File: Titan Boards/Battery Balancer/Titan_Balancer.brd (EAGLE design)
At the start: 101.6 x 101.6 mm, 86 parts, among them IC1 REG1117, P1 39-30-04?, P2 39-30-10?, P3 39-30-10?, Q1 SPD30P06PTO252, Q12 310mA/60V/1.6Ω, Q2 SPB80P06P, Q3 SPB80P06P, Q4 SPD30P06PTO252, U1 I6A4W020A033V-001-R, U2 I6A4W020A033V-001-R

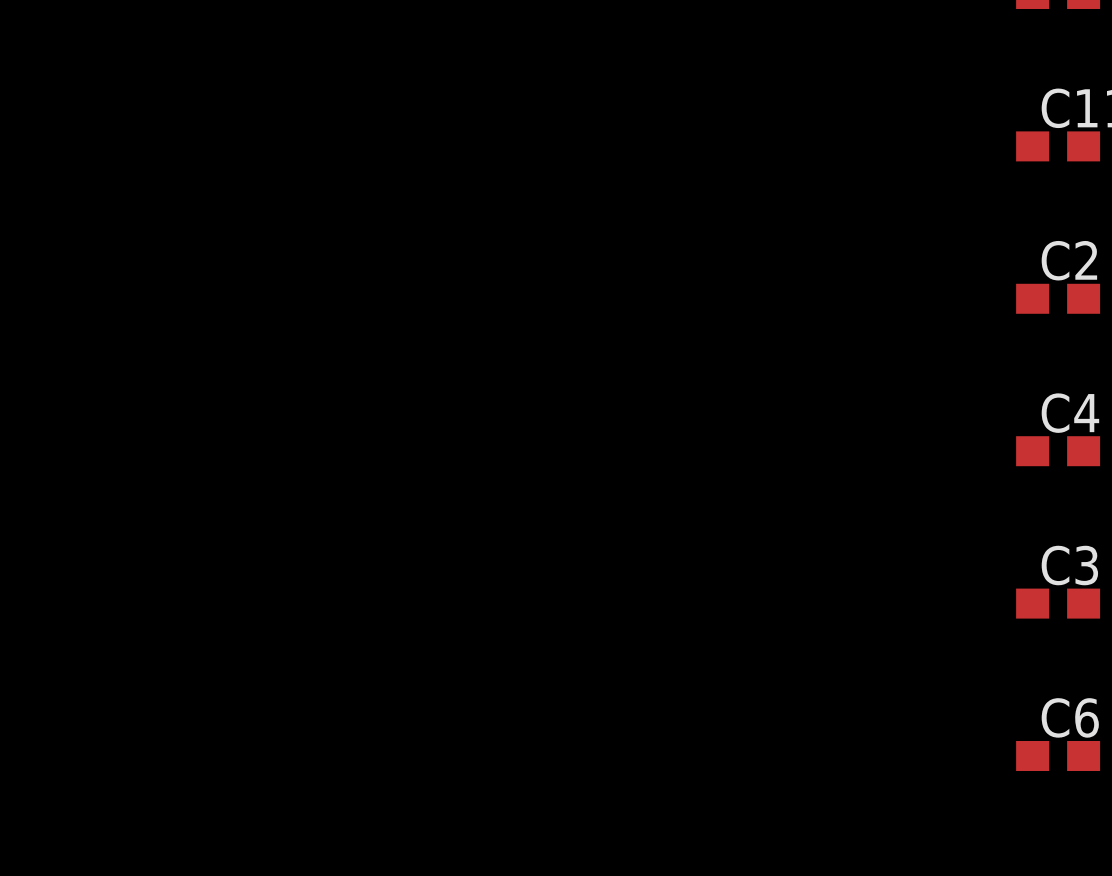
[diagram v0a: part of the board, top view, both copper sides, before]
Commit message: Seperated fan and lighting and added web addresses
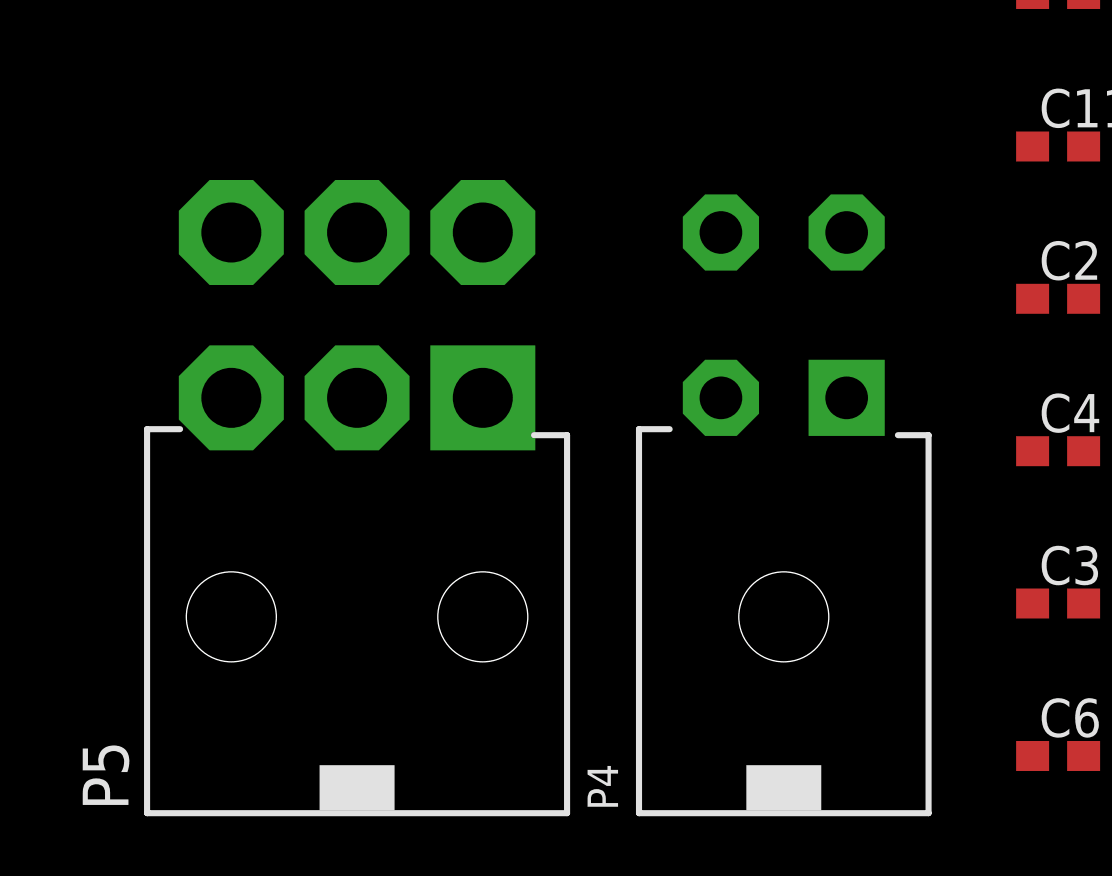
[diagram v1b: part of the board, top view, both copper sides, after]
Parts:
- added P4: 39-30-04?, con-molex-mini-fit:39-30-?04?
- added P5: 39-30-06?, con-molex-mini-fit:39-30-?06?
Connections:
- new net LIGHTING_1.1: P5.1
- new net LIGHTING_2.1: P5.6
- net +12V: now also P5.2, P5.3, P5.4, P5.5
- net GND: now also P4.1, P4.2, P4.3, P4.4
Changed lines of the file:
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@@
 <attribute name="VALUE" x="0.889" y="-187.833" size="1.27" layer="27"/>
+</element>
+<element name="P4" library="con-molex-mini-fit" package="39-30-?04?" value="39-30-04?" x="-7.62" y="-173.99" smashed="yes">
+<attribute name="NAME" x="-13.1445" y="-187.7441" size="1.016" layer="25" ratio="18" rot="R90"/>
+<attribute name="VALUE" x="-0.8255" y="-187.7441" size="1.016" layer="27" ratio="10" rot="R90"/>
+</element>
+<element name="P5" library="con-molex-mini-fit" package="39-30-?06?" value="39-30-06?" x="-21.844" y="-173.99" smashed="yes">
+<attribute name="NAME" x="-29.464" y="-187.7441" size="1.524" layer="21" ratio="18" rot="R90"/>
 </element>
 </elements>
@@
 <contactref element="C3" pad="2"/>
 <contactref element="C6" pad="1"/>
+<contactref element="P4" pad="1"/>
+<contactref element="P4" pad="3"/>
+<contactref element="P4" pad="4"/>
+<contactref element="P4" pad="2"/>
 <wire x1="163.488" y1="79.756" x2="171.13" y2="79.518" width="0" layer="19" extent="1-1"/>
 <wire x1="151.13" y1="79.3242" x2="163.488" y2="79.756" width="0" layer="19" extent="1-1"/>
@@
 <wire x1="2.374" y1="-180.848" x2="2.374" y2="-175.768" width="0" layer="19" extent="1-1"/>
 <wire x1="0.674" y1="-185.928" x2="2.374" y2="-180.848" width="0" layer="19" extent="1-1"/>
+<wire x1="-5.5245" y1="-173.99" x2="2.374" y2="-175.768" width="0" layer="19" extent="1-1"/>
+<wire x1="-9.7155" y1="-173.99" x2="-5.5245" y2="-173.99" width="0" layer="19" extent="1-1"/>
+<wire x1="-9.7155" y1="-168.4782" x2="-9.7155" y2="-173.99" width="0" layer="19" extent="1-1"/>
+<wire x1="-5.5245" y1="-168.4782" x2="-9.7155" y2="-168.4782" width="0" layer="19" extent="1-1"/>
 </signal>
 <signal name="+5V">
@@
 <contactref element="C7" pad="1"/>
 <contactref element="C8" pad="1"/>
+<contactref element="P5" pad="4"/>
+<contactref element="P5" pad="2"/>
+<contactref element="P5" pad="3"/>
+<contactref element="P5" pad="5"/>
+<wire x1="-21.844" y1="-173.99" x2="-26.035" y2="-173.99" width="0" layer="19" extent="1-1"/>
+<wire x1="-21.844" y1="-168.4782" x2="-21.844" y2="-173.99" width="0" layer="19" extent="1-1"/>
+<wire x1="-17.653" y1="-168.4782" x2="-21.844" y2="-168.4782" width="0" layer="19" extent="1-1"/>
+<wire x1="0.674" y1="-150.368" x2="-17.653" y2="-168.4782" width="0" layer="19" extent="1-1"/>
 <wire x1="0.674" y1="-145.288" x2="0.674" y2="-150.368" width="0" layer="19" extent="1-1"/>
 <wire x1="0.674" y1="-140.208" x2="0.674" y2="-145.288" width="0" layer="19" extent="1-1"/>
@@
 <wire x1="2.3622" y1="36.83" x2="72.4615" y2="3.423" width="0" layer="19" extent="1-1"/>
 </signal>
+<signal name="LIGHTING_2.1">
+<contactref element="P5" pad="6"/>
+</signal>
+<signal name="LIGHTING_1.1">
+<contactref element="P5" pad="1"/>
+</signal>
 </signals>

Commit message: fixed connectors
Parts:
- removed P3: 39-30-10?, con-molex-mini-fit:39-30-?10?
- moved P4 254.8 mm to (-23.6, 80.3)
- moved P5 200.0 mm to (-52.8, 23.6)
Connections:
- removed net LIGHTING_1.1: P5.1
- removed net LIGHTING_2.1: P5.6
- net +12V: now also P4.1, P4.3; no longer P3.2, P3.3, P3.4, P3.5, P5.2, P5.4
- net GND: now also P5.2, P5.4; no longer P3.10, P3.7, P3.8, P3.9, P4.1, P4.3
- net LIGHTING_1: now also P5.1; no longer P3.1
- net LIGHTING_2: now also P5.6; no longer P3.6

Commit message: changed wiring on fan and lighting and more data sheet links
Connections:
- net +12V: now also P4.2, P5.2; no longer P4.3, P5.5
- net GND: now also P4.3, P5.5, P5.6; no longer P4.2, P5.2, P5.4
- net LIGHTING_2: now also P5.4; no longer P5.6
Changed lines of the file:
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@@
 <?xml version="1.0" encoding="utf-8"?>
 <!DOCTYPE eagle SYSTEM "eagle.dtd">
-<eagle version="9.5.2">
+<eagle version="9.6.2">
 <drawing>
 <settings>
@@
 <contactref element="C6" pad="1"/>
 <contactref element="P4" pad="4"/>
-<contactref element="P4" pad="2"/>
-<contactref element="P5" pad="2"/>
-<contactref element="P5" pad="4"/>
+<contactref element="P4" pad="3"/>
+<contactref element="P5" pad="5"/>
+<contactref element="P5" pad="6"/>
 <wire x1="163.488" y1="79.756" x2="171.13" y2="79.518" width="0" layer="19" extent="1-1"/>
 <wire x1="151.13" y1="79.3242" x2="163.488" y2="79.756" width="0" layer="19" extent="1-1"/>
@@
 <wire x1="2.3622" y1="50.4825" x2="2.3622" y2="54.6735" width="0" layer="19" extent="1-1"/>
 <wire x1="2.3622" y1="46.2915" x2="2.3622" y2="50.4825" width="0" layer="19" extent="1-1"/>
+<wire x1="-21.5265" y1="85.7758" x2="2.3622" y2="75.6285" width="0" layer="19" extent="1-1"/>
+<wire x1="-25.7175" y1="85.7758" x2="-21.5265" y2="85.7758" width="0" layer="19" extent="1-1"/>
 <wire x1="95.484" y1="24.658" x2="95.484" y2="52.558" width="0" layer="19" extent="1-1"/>
 <wire x1="36.4998" y1="36.83" x2="2.3622" y2="46.2915" width="0" layer="19" extent="1-1"/>
@@
 <wire x1="2.374" y1="-180.848" x2="2.374" y2="-175.768" width="0" layer="19" extent="1-1"/>
 <wire x1="0.674" y1="-185.928" x2="2.374" y2="-180.848" width="0" layer="19" extent="1-1"/>
-<wire x1="-25.7175" y1="80.264" x2="2.374" y2="-175.768" width="0" layer="19" extent="1-1"/>
-<wire x1="-25.7175" y1="85.7758" x2="-25.7175" y2="80.264" width="0" layer="19" extent="1-1"/>
-<wire x1="-48.641" y1="29.1338" x2="-25.7175" y2="85.7758" width="0" layer="19" extent="1-1"/>
-<wire x1="-52.832" y1="23.622" x2="-48.641" y2="29.1338" width="0" layer="19" extent="1-1"/>
+<wire x1="-52.832" y1="29.1338" x2="2.3622" y2="46.2915" width="0" layer="19" extent="1-1"/>
+<wire x1="-57.023" y1="29.1338" x2="-52.832" y2="29.1338" width="0" layer="19" extent="1-1"/>
 </signal>
 <signal name="+5V">
@@
 <contactref element="C7" pad="1"/>
 <contactref element="C8" pad="1"/>
-<contactref element="P5" pad="3"/>
-<contactref element="P5" pad="5"/>
 <contactref element="P4" pad="1"/>
-<contactref element="P4" pad="3"/>
-<wire x1="-52.832" y1="29.1338" x2="-57.023" y2="23.622" width="0" layer="19" extent="1-1"/>
-<wire x1="-21.5265" y1="85.7758" x2="-52.832" y2="29.1338" width="0" layer="19" extent="1-1"/>
-<wire x1="-21.5265" y1="80.264" x2="-21.5265" y2="85.7758" width="0" layer="19" extent="1-1"/>
-<wire x1="0.674" y1="-150.368" x2="-21.5265" y2="85.7758" width="0" layer="19" extent="1-1"/>
+<contactref element="P4" pad="2"/>
+<contactref element="P5" pad="3"/>
+<contactref element="P5" pad="2"/>
 <wire x1="0.674" y1="-145.288" x2="0.674" y2="-150.368" width="0" layer="19" extent="1-1"/>
 <wire x1="0.674" y1="-140.208" x2="0.674" y2="-145.288" width="0" layer="19" extent="1-1"/>
@@
 <wire x1="84.084" y1="24.658" x2="80.284" y2="24.658" width="0" layer="19" extent="1-1"/>
 <wire x1="87.116" y1="35.332" x2="84.084" y2="24.658" width="0" layer="19" extent="1-1"/>
+<wire x1="-21.5265" y1="80.264" x2="30.988" y2="36.83" width="0" layer="19" extent="1-1"/>
+<wire x1="-25.7175" y1="80.264" x2="-21.5265" y2="80.264" width="0" layer="19" extent="1-1"/>
+<wire x1="-52.832" y1="23.622" x2="-25.7175" y2="80.264" width="0" layer="19" extent="1-1"/>
+<wire x1="-57.023" y1="23.622" x2="-52.832" y2="23.622" width="0" layer="19" extent="1-1"/>
 </signal>
 <signal name="BALANCED_OUT">
@@
 <contactref element="U$1" pad="33"/>
 <contactref element="P5" pad="1"/>
-<wire x1="75.0015" y1="3.423" x2="-48.641" y2="23.622" width="0" layer="19" extent="1-1"/>
+<wire x1="-48.641" y1="23.622" x2="75.0015" y2="3.423" width="0" layer="19" extent="1-1"/>
 </signal>
 <signal name="LIGHTING_2">
 <contactref element="U$1" pad="34"/>
-<contactref element="P5" pad="6"/>
-<wire x1="72.4615" y1="3.423" x2="-57.023" y2="29.1338" width="0" layer="19" extent="1-1"/>
+<contactref element="P5" pad="4"/>
+<wire x1="-48.641" y1="29.1338" x2="72.4615" y2="3.423" width="0" layer="19" extent="1-1"/>
 </signal>
 </signals>

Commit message: Fixed R1, Flipped a connector on the board, and moved components around off the board to easier tell what is connected
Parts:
- moved R23 218.5 mm to (176.5, 29.7)
- moved R17 214.4 mm to (164.6, 43.2)
- moved R16 211.2 mm to (169.7, 36.8)
- moved R11 117.1 mm to (3.05, -156.7)
- moved Q1 65.8 mm to (36.1, 36.1)
- moved LED1 57.4 mm to (182.9, 75.7)
- moved BALANCED 56.9 mm to (172.0, 72.9)
- moved PORT 52.5 mm to (165.4, 65.3)
- moved 12V 46.7 mm to (173.7, 38.4), flipped to the bottom
- moved Q12 44.6 mm to (187.7, 75.2)
- moved R20 44.3 mm to (-5.59, -148.3)
- moved FAULT_LED 42.1 mm to (170.9, 27.7)
- moved 5V 41.0 mm to (169.7, 45.2), flipped to the bottom
- moved 3V3 40.1 mm to (168.4, 51.3)
- moved U$9 36.9 mm to (145.3, 1.52)
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
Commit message: Rearranged LED layout
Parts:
- R23: value (none) -> 30
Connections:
- removed net N$30: 3V3.C, Q10.1
- new net N$9: BALANCED.C, Q10.1
- net N$29: now also 3V3.C; no longer BALANCED.C
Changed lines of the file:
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@@
 <?xml version="1.0" encoding="utf-8"?>
 <!DOCTYPE eagle SYSTEM "eagle.dtd">
-<eagle version="9.6.2">
+<eagle version="9.5.2">
 <drawing>
 <settings>
@@
 <attribute name="VALUE" x="163.957" y="41.275" size="1.27" layer="27"/>
 </element>
-<element name="R23" library="rcl" library_urn="urn:adsk.eagle:library:334" package="R0603" package3d_urn="urn:adsk.eagle:package:23555/3" value="" x="176.53" y="29.718" smashed="yes">
+<element name="R23" library="rcl" library_urn="urn:adsk.eagle:library:334" package="R0603" package3d_urn="urn:adsk.eagle:package:23555/3" value="30" x="176.53" y="29.718" smashed="yes">
 <attribute name="NAME" x="175.895" y="30.353" size="1.27" layer="25"/>
 <attribute name="POPULARITY" value="77" x="176.53" y="29.718" size="1.778" layer="27" display="off"/>
@@
 </signal>
 <signal name="N$29">
-<contactref element="BALANCED" pad="C"/>
 <contactref element="Q7" pad="3"/>
-<wire x1="171.208" y1="72.898" x2="169.672" y2="67.902" width="0" layer="19" extent="1-1"/>
-</signal>
-<signal name="N$30">
 <contactref element="3V3" pad="C"/>
-<contactref element="Q10" pad="1"/>
-<wire x1="167.652" y1="51.308" x2="173.04" y2="54.272" width="0" layer="19" extent="1-1"/>
+<wire x1="167.652" y1="51.308" x2="169.672" y2="67.902" width="0" layer="19" extent="1-1"/>
 </signal>
 <signal name="N$31">
@@
 <wire x1="-48.641" y1="29.1338" x2="72.4615" y2="3.423" width="0" layer="19" extent="1-1"/>
 </signal>
+<signal name="N$9">
+<contactref element="BALANCED" pad="C"/>
+<contactref element="Q10" pad="1"/>
+<wire x1="173.04" y1="54.272" x2="171.208" y2="72.898" width="0" layer="19" extent="1-1"/>
+</signal>
 </signals>

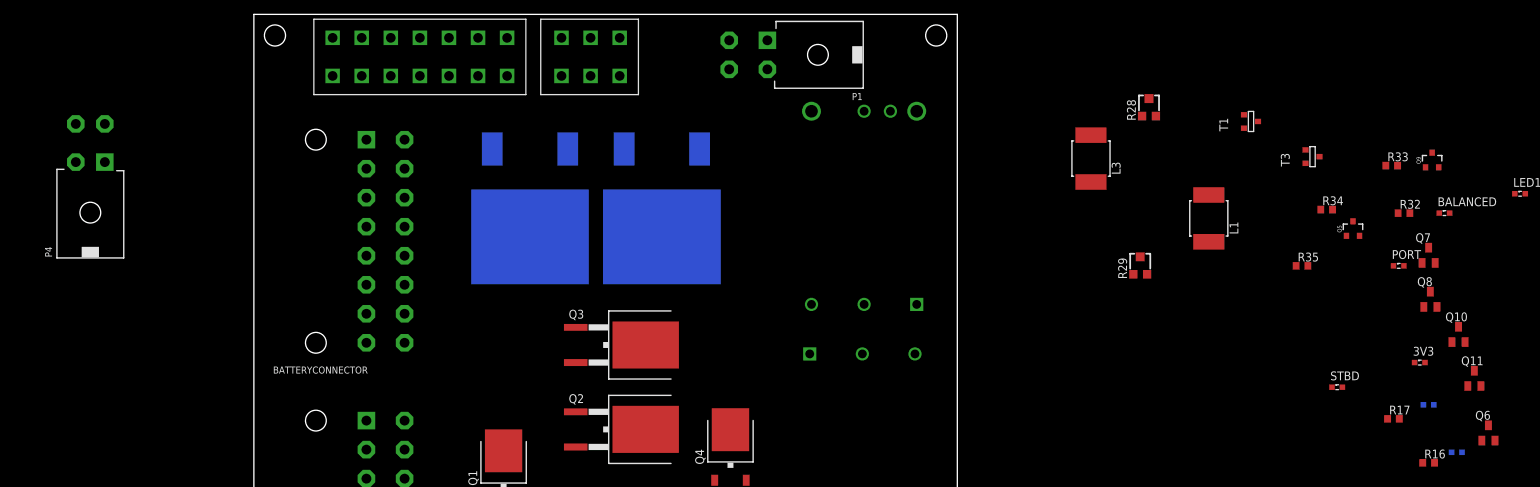
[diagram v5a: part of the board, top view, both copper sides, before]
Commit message: Changed LED layout going to alter for AND and Inverters
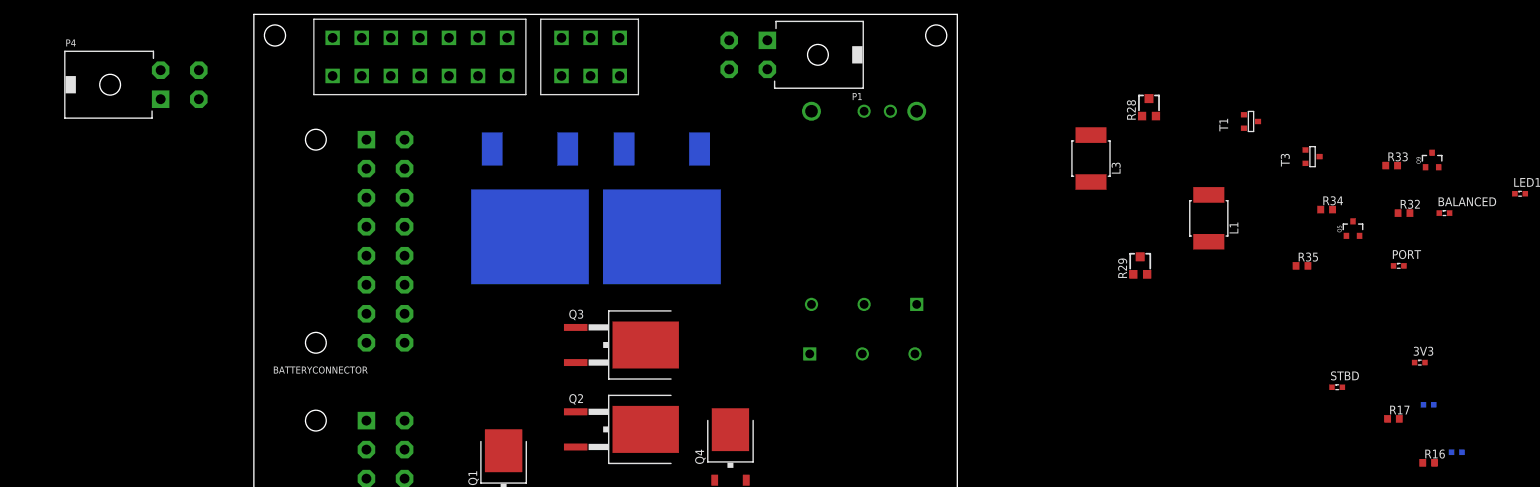
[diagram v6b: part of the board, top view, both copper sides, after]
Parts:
- removed Q10, Q11, Q6, Q7, Q8: (no value), semicon-smd-ipc:SOT23
- 12V, 3V3, 5V, BALANCED, PORT, STBD: value (none) -> RED
- FAULT_LED: value (none) -> GREEN
- R23: value 30 -> 95
- moved P4 15.1 mm to (-13.5, 91.4), turned to 270 degrees
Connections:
- removed net N$20: 12V.C, Q6.1
- removed net N$26: 5V.C, Q11.1
- removed net N$27: PORT.C, Q7.1
- removed net N$28: Q8.1, STBD.C
- removed net N$29: 3V3.C, Q7.3
- removed net N$31: Q11.2, Q6.3
- removed net N$32: Q10.2, Q11.3
- removed net N$33: Q7.2, Q8.3
- removed net N$34: Q10.3, Q8.2
- removed net N$9: BALANCED.C, Q10.1
- net 12V_LED: no longer 12V.A
- net 3V3_LED: no longer 3V3.A
- net 5V_LED: no longer 5V.A
- net BALANCED_LED: no longer BALANCED.A
- net N$1: no longer Q6.2
- net PORT_LED: no longer PORT.A
- net STBD_LED: no longer STBD.A

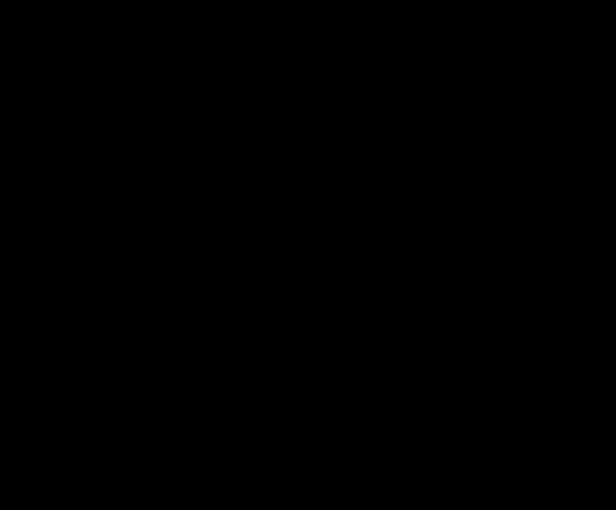
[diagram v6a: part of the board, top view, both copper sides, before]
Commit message: added AND IC to library and schematic
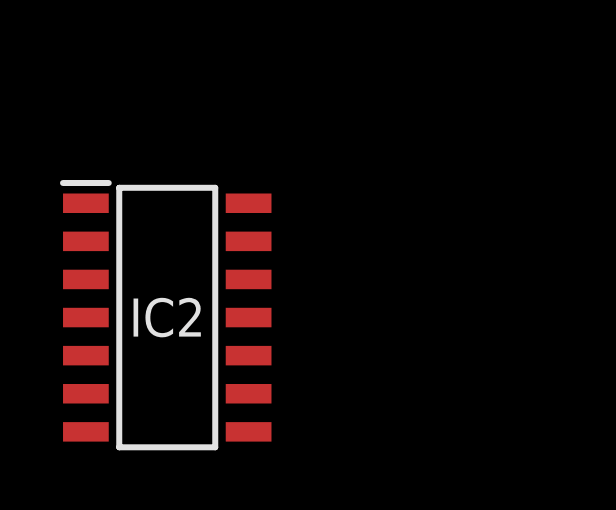
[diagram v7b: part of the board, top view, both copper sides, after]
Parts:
- added IC2: SN74LV11AD, SN74LV11AD:SOIC127P600X175-14N
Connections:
- new net N$20: 5V.A
- new net N$26: BALANCED.A
- new net N$27: STBD.A
- new net N$28: PORT.A
- new net N$29: 3V3.A
- new net N$30: IC2.11, IC2.12
- new net N$9: 12V.A
- net +5V: now also IC2.14
- net GND: now also IC2.7
